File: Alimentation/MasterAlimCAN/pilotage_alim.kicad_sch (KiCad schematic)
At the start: 4 parts, among them U4 74LVC1G02

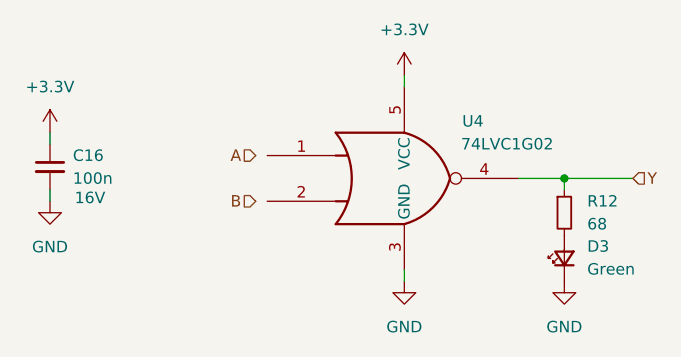
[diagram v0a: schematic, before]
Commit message: Restructure schematics of AlimCAN
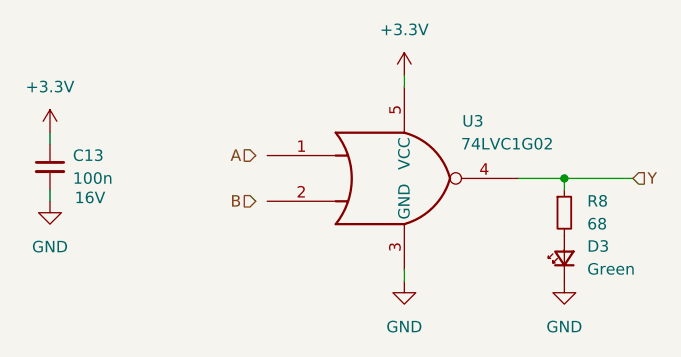
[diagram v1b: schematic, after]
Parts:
- renumbered C16 to C13, R12 to R8, U4 to U3
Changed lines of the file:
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@@
   (symbol (lib_id "power:GND") (at 246.38 123.19 0) (unit 1)
     (in_bom yes) (on_board yes) (dnp no) (fields_autoplaced)
-    (property "Reference" "#PWR053" (at 246.38 129.54 0)
+    (property "Reference" "#PWR035" (at 246.38 129.54 0)
       (effects (font (size 1.27 1.27)) hide)
     )
@@
     (instances
       (project "MasterAlimCAN"
-        (path "/c83bc042-587c-48f9-abdb-41233c8ec938/a6f4e771-72c9-4983-80a1-8951328e7346"
-          (reference "#PWR053") (unit 1)
-        )
-        (path "/c83bc042-587c-48f9-abdb-41233c8ec938/e65f16f5-16c4-48e9-9c3f-07516aed1840"
-          (reference "#PWR053") (unit 1)
-        )
-        (path "/c83bc042-587c-48f9-abdb-41233c8ec938/437897c5-9bcb-4226-b09d-80613b2e8e00"
-          (reference "#PWR053") (unit 1)
+        (path "/c83bc042-587c-48f9-abdb-41233c8ec938/2257b505-9461-4792-8707-8d13b64ba796/ef164321-3fd7-4989-9796-e8f2716b1c85"
+          (reference "#PWR035") (unit 1)
+        )
+        (path "/c83bc042-587c-48f9-abdb-41233c8ec938/2257b505-9461-4792-8707-8d13b64ba796/b62c8685-6929-45de-9238-6177db5cd56b"
+          (reference "#PWR040") (unit 1)
         )
       )
@@
   (symbol (lib_id "power:+3.3V") (at 189.23 106.68 0) (unit 1)
     (in_bom yes) (on_board yes) (dnp no) (fields_autoplaced)
-    (property "Reference" "#PWR049" (at 189.23 110.49 0)
+    (property "Reference" "#PWR031" (at 189.23 110.49 0)
       (effects (font (size 1.27 1.27)) hide)
     )
@@
     (instances
       (project "MasterAlimCAN"
-        (path "/c83bc042-587c-48f9-abdb-41233c8ec938/a6f4e771-72c9-4983-80a1-8951328e7346"
-          (reference "#PWR049") (unit 1)
-        )
-        (path "/c83bc042-587c-48f9-abdb-41233c8ec938/e65f16f5-16c4-48e9-9c3f-07516aed1840"
-          (reference "#PWR049") (unit 1)
-        )
-        (path "/c83bc042-587c-48f9-abdb-41233c8ec938/437897c5-9bcb-4226-b09d-80613b2e8e00"
-          (reference "#PWR049") (unit 1)
+        (path "/c83bc042-587c-48f9-abdb-41233c8ec938/2257b505-9461-4792-8707-8d13b64ba796/ef164321-3fd7-4989-9796-e8f2716b1c85"
+          (reference "#PWR031") (unit 1)
+        )
+        (path "/c83bc042-587c-48f9-abdb-41233c8ec938/2257b505-9461-4792-8707-8d13b64ba796/b62c8685-6929-45de-9238-6177db5cd56b"
+          (reference "#PWR036") (unit 1)
         )
       )
@@
   (symbol (lib_id "Device:R_Small") (at 246.38 115.57 0) (unit 1)
     (in_bom yes) (on_board yes) (dnp no) (fields_autoplaced)
-    (property "Reference" "R12" (at 248.92 114.3 0)
+    (property "Reference" "R8" (at 248.92 114.3 0)
       (effects (font (size 1.27 1.27)) (justify left))
     )
@@
     (instances
       (project "MasterAlimCAN"
-        (path "/c83bc042-587c-48f9-abdb-41233c8ec938/a6f4e771-72c9-4983-80a1-8951328e7346"
-          (reference "R12") (unit 1)
-        )
-        (path "/c83bc042-587c-48f9-abdb-41233c8ec938/437897c5-9bcb-4226-b09d-80613b2e8e00"
-          (reference "R12") (unit 1)
-        )
-        (path "/c83bc042-587c-48f9-abdb-41233c8ec938/e65f16f5-16c4-48e9-9c3f-07516aed1840"
-          (reference "R12") (unit 1)
+        (path "/c83bc042-587c-48f9-abdb-41233c8ec938/2257b505-9461-4792-8707-8d13b64ba796/ef164321-3fd7-4989-9796-e8f2716b1c85"
+          (reference "R8") (unit 1)
+        )
+        (path "/c83bc042-587c-48f9-abdb-41233c8ec938/2257b505-9461-4792-8707-8d13b64ba796/b62c8685-6929-45de-9238-6177db5cd56b"
+          (reference "R9") (unit 1)
         )
       )
@@
   (symbol (lib_id "power:GND") (at 228.6 123.19 0) (unit 1)
     (in_bom yes) (on_board yes) (dnp no) (fields_autoplaced)
-    (property "Reference" "#PWR052" (at 228.6 129.54 0)
+    (property "Reference" "#PWR034" (at 228.6 129.54 0)
       (effects (font (size 1.27 1.27)) hide)
     )
@@
     (instances
       (project "MasterAlimCAN"
-        (path "/c83bc042-587c-48f9-abdb-41233c8ec938/a6f4e771-72c9-4983-80a1-8951328e7346"
-          (reference "#PWR052") (unit 1)
-        )
-        (path "/c83bc042-587c-48f9-abdb-41233c8ec938/e65f16f5-16c4-48e9-9c3f-07516aed1840"
-          (reference "#PWR052") (unit 1)
-        )
-        (path "/c83bc042-587c-48f9-abdb-41233c8ec938/437897c5-9bcb-4226-b09d-80613b2e8e00"
-          (reference "#PWR052") (unit 1)
+        (path "/c83bc042-587c-48f9-abdb-41233c8ec938/2257b505-9461-4792-8707-8d13b64ba796/ef164321-3fd7-4989-9796-e8f2716b1c85"
+          (reference "#PWR034") (unit 1)
+        )
+        (path "/c83bc042-587c-48f9-abdb-41233c8ec938/2257b505-9461-4792-8707-8d13b64ba796/b62c8685-6929-45de-9238-6177db5cd56b"
+          (reference "#PWR039") (unit 1)
         )
       )
@@
   (symbol (lib_id "74xGxx:74LVC1G02") (at 228.6 111.76 0) (unit 1)
     (in_bom yes) (on_board yes) (dnp no)
-    (property "Reference" "U4" (at 236.22 105.41 0)
+    (property "Reference" "U3" (at 236.22 105.41 0)
       (effects (font (size 1.27 1.27)))
     )
@@
     (instances
       (project "MasterAlimCAN"
-        (path "/c83bc042-587c-48f9-abdb-41233c8ec938/a6f4e771-72c9-4983-80a1-8951328e7346"
-          (reference "U4") (unit 1)
-        )
-        (path "/c83bc042-587c-48f9-abdb-41233c8ec938/e65f16f5-16c4-48e9-9c3f-07516aed1840"
-          (reference "U4") (unit 1)
-        )
-        (path "/c83bc042-587c-48f9-abdb-41233c8ec938/437897c5-9bcb-4226-b09d-80613b2e8e00"
+        (path "/c83bc042-587c-48f9-abdb-41233c8ec938/2257b505-9461-4792-8707-8d13b64ba796/ef164321-3fd7-4989-9796-e8f2716b1c85"
+          (reference "U3") (unit 1)
+        )
+        (path "/c83bc042-587c-48f9-abdb-41233c8ec938/2257b505-9461-4792-8707-8d13b64ba796/b62c8685-6929-45de-9238-6177db5cd56b"
           (reference "U4") (unit 1)
         )
@@
     (instances
       (project "MasterAlimCAN"
-        (path "/c83bc042-587c-48f9-abdb-41233c8ec938/a6f4e771-72c9-4983-80a1-8951328e7346"
+        (path "/c83bc042-587c-48f9-abdb-41233c8ec938/2257b505-9461-4792-8707-8d13b64ba796/ef164321-3fd7-4989-9796-e8f2716b1c85"
           (reference "D3") (unit 1)
         )
-        (path "/c83bc042-587c-48f9-abdb-41233c8ec938/437897c5-9bcb-4226-b09d-80613b2e8e00"
-          (reference "D3") (unit 1)
-        )
-        (path "/c83bc042-587c-48f9-abdb-41233c8ec938/e65f16f5-16c4-48e9-9c3f-07516aed1840"
-          (reference "D3") (unit 1)
+        (path "/c83bc042-587c-48f9-abdb-41233c8ec938/2257b505-9461-4792-8707-8d13b64ba796/b62c8685-6929-45de-9238-6177db5cd56b"
+          (reference "D4") (unit 1)
         )
       )
@@
   (symbol (lib_id "power:+3.3V") (at 228.6 100.33 0) (unit 1)
     (in_bom yes) (on_board yes) (dnp no) (fields_autoplaced)
-    (property "Reference" "#PWR051" (at 228.6 104.14 0)
+    (property "Reference" "#PWR033" (at 228.6 104.14 0)
       (effects (font (size 1.27 1.27)) hide)
     )
@@
     (instances
       (project "MasterAlimCAN"
-        (path "/c83bc042-587c-48f9-abdb-41233c8ec938/a6f4e771-72c9-4983-80a1-8951328e7346"
-          (reference "#PWR051") (unit 1)
-        )
-        (path "/c83bc042-587c-48f9-abdb-41233c8ec938/e65f16f5-16c4-48e9-9c3f-07516aed1840"
-          (reference "#PWR051") (unit 1)
-        )
-        (path "/c83bc042-587c-48f9-abdb-41233c8ec938/437897c5-9bcb-4226-b09d-80613b2e8e00"
-          (reference "#PWR051") (unit 1)
+        (path "/c83bc042-587c-48f9-abdb-41233c8ec938/2257b505-9461-4792-8707-8d13b64ba796/ef164321-3fd7-4989-9796-e8f2716b1c85"
+          (reference "#PWR033") (unit 1)
+        )
+        (path "/c83bc042-587c-48f9-abdb-41233c8ec938/2257b505-9461-4792-8707-8d13b64ba796/b62c8685-6929-45de-9238-6177db5cd56b"
+          (reference "#PWR038") (unit 1)
         )
       )
@@
   (symbol (lib_id "Device:C_Small") (at 189.23 110.49 0) (unit 1)
     (in_bom yes) (on_board yes) (dnp no)
-    (property "Reference" "C16" (at 191.77 109.2263 0)
+    (property "Reference" "C13" (at 191.77 109.2263 0)
       (effects (font (size 1.27 1.27)) (justify left))
     )
@@
     (instances
       (project "MasterAlimCAN"
-        (path "/c83bc042-587c-48f9-abdb-41233c8ec938/a6f4e771-72c9-4983-80a1-8951328e7346"
-          (reference "C16") (unit 1)
-        )
-        (path "/c83bc042-587c-48f9-abdb-41233c8ec938/437897c5-9bcb-4226-b09d-80613b2e8e00"
-          (reference "C16") (unit 1)
-        )
-        (path "/c83bc042-587c-48f9-abdb-41233c8ec938/e65f16f5-16c4-48e9-9c3f-07516aed1840"
-          (reference "C16") (unit 1)
+        (path "/c83bc042-587c-48f9-abdb-41233c8ec938/2257b505-9461-4792-8707-8d13b64ba796/ef164321-3fd7-4989-9796-e8f2716b1c85"
+          (reference "C13") (unit 1)
+        )
+        (path "/c83bc042-587c-48f9-abdb-41233c8ec938/2257b505-9461-4792-8707-8d13b64ba796/b62c8685-6929-45de-9238-6177db5cd56b"
+          (reference "C14") (unit 1)
         )
       )
@@
   (symbol (lib_id "power:GND") (at 189.23 114.3 0) (unit 1)
     (in_bom yes) (on_board yes) (dnp no) (fields_autoplaced)
-    (property "Reference" "#PWR050" (at 189.23 120.65 0)
+    (property "Reference" "#PWR032" (at 189.23 120.65 0)
       (effects (font (size 1.27 1.27)) hide)
     )
@@
     (instances
       (project "MasterAlimCAN"
-        (path "/c83bc042-587c-48f9-abdb-41233c8ec938/a6f4e771-72c9-4983-80a1-8951328e7346"
-          (reference "#PWR050") (unit 1)
-        )
-        (path "/c83bc042-587c-48f9-abdb-41233c8ec938/e65f16f5-16c4-48e9-9c3f-07516aed1840"
-          (reference "#PWR050") (unit 1)
-        )
-        (path "/c83bc042-587c-48f9-abdb-41233c8ec938/437897c5-9bcb-4226-b09d-80613b2e8e00"
-          (reference "#PWR050") (unit 1)
-        )
-      )
+        (path "/c83bc042-587c-48f9-abdb-41233c8ec938/2257b505-9461-4792-8707-8d13b64ba796/ef164321-3fd7-4989-9796-e8f2716b1c85"
+          (reference "#PWR032") (unit 1)
+        )
+        (path "/c83bc042-587c-48f9-abdb-41233c8ec938/2257b505-9461-4792-8707-8d13b64ba796/b62c8685-6929-45de-9238-6177db5cd56b"
+          (reference "#PWR037") (unit 1)
+        )
+      )

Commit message: Init placement for MasterAlimCAN
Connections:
- net A: now also U3.1
- net B: now also U3.2
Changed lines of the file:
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@@
+    (stroke (width 0) (type default))
+  )
+  (wire (pts (xy 212.09 114.3) (xy 213.36 114.3))
+    (stroke (width 0) (type default))
+  )
+  (wire (pts (xy 212.09 109.22) (xy 213.36 109.22))
     (stroke (width 0) (type default))
   )
@@
   (symbol (lib_id "power:GND") (at 246.38 123.19 0) (unit 1)
     (in_bom yes) (on_board yes) (dnp no) (fields_autoplaced)
-    (property "Reference" "#PWR035" (at 246.38 129.54 0)
+    (property "Reference" "#PWR037" (at 246.38 129.54 0)
       (effects (font (size 1.27 1.27)) hide)
     )
@@
       (project "MasterAlimCAN"
         (path "/c83bc042-587c-48f9-abdb-41233c8ec938/2257b505-9461-4792-8707-8d13b64ba796/ef164321-3fd7-4989-9796-e8f2716b1c85"
-          (reference "#PWR035") (unit 1)
-        )
-        (path "/c83bc042-587c-48f9-abdb-41233c8ec938/2257b505-9461-4792-8707-8d13b64ba796/b62c8685-6929-45de-9238-6177db5cd56b"
-          (reference "#PWR040") (unit 1)
+          (reference "#PWR037") (unit 1)
+        )
+        (path "/c83bc042-587c-48f9-abdb-41233c8ec938/2257b505-9461-4792-8707-8d13b64ba796/b62c8685-6929-45de-9238-6177db5cd56b"
+          (reference "#PWR042") (unit 1)
         )
       )
@@
   (symbol (lib_id "power:+3.3V") (at 189.23 106.68 0) (unit 1)
     (in_bom yes) (on_board yes) (dnp no) (fields_autoplaced)
-    (property "Reference" "#PWR031" (at 189.23 110.49 0)
+    (property "Reference" "#PWR033" (at 189.23 110.49 0)
       (effects (font (size 1.27 1.27)) hide)
     )
@@
       (project "MasterAlimCAN"
         (path "/c83bc042-587c-48f9-abdb-41233c8ec938/2257b505-9461-4792-8707-8d13b64ba796/ef164321-3fd7-4989-9796-e8f2716b1c85"
-          (reference "#PWR031") (unit 1)
-        )
-        (path "/c83bc042-587c-48f9-abdb-41233c8ec938/2257b505-9461-4792-8707-8d13b64ba796/b62c8685-6929-45de-9238-6177db5cd56b"
+          (reference "#PWR033") (unit 1)
+        )
+        (path "/c83bc042-587c-48f9-abdb-41233c8ec938/2257b505-9461-4792-8707-8d13b64ba796/b62c8685-6929-45de-9238-6177db5cd56b"
+          (reference "#PWR038") (unit 1)
+        )
+      )
+    )
+  )
+  (symbol (lib_id "Device:R_Small") (at 246.38 115.57 0) (unit 1)
+    (in_bom yes) (on_board yes) (dnp no) (fields_autoplaced)
+    (property "Reference" "R8" (at 248.92 114.3 0)
+      (effects (font (size 1.27 1.27)) (justify left))
+    )
+    (property "Value" "68" (at 248.92 116.84 0)
+      (effects (font (size 1.27 1.27)) (justify left))
+    )
+    (property "Footprint" "Resistor_SMD:R_0805_2012Metric_Pad1.20x1.40mm_HandSolder" (at 246.38 115.57 0)
+      (effects (font (size 1.27 1.27)) hide)
+    )
+    (property "Datasheet" "~" (at 246.38 115.57 0)
+      (effects (font (size 1.27 1.27)) hide)
+    )
+    (property "LCSC Part" "C17802" (at 246.38 115.57 0)
+      (effects (font (size 1.27 1.27)) hide)
+    )
+    (pin "2")
+    (pin "1")
+    (instances
+      (project "MasterAlimCAN"
+        (path "/c83bc042-587c-48f9-abdb-41233c8ec938/2257b505-9461-4792-8707-8d13b64ba796/ef164321-3fd7-4989-9796-e8f2716b1c85"
+          (reference "R8") (unit 1)
+        )
+        (path "/c83bc042-587c-48f9-abdb-41233c8ec938/2257b505-9461-4792-8707-8d13b64ba796/b62c8685-6929-45de-9238-6177db5cd56b"
+          (reference "R9") (unit 1)
+        )
+      )
+    )
+  )
+  (symbol (lib_id "power:GND") (at 228.6 123.19 0) (unit 1)
+    (in_bom yes) (on_board yes) (dnp no) (fields_autoplaced)
+    (property "Reference" "#PWR036" (at 228.6 129.54 0)
+      (effects (font (size 1.27 1.27)) hide)
+    )
+    (property "Value" "GND" (at 228.6 128.27 0)
+      (effects (font (size 1.27 1.27)))
+    )
+    (property "Footprint" "" (at 228.6 123.19 0)
+      (effects (font (size 1.27 1.27)) hide)
+    )
+    (property "Datasheet" "" (at 228.6 123.19 0)
+      (effects (font (size 1.27 1.27)) hide)
+    )
+    (pin "1")
+    (instances
+      (project "MasterAlimCAN"
+        (path "/c83bc042-587c-48f9-abdb-41233c8ec938/2257b505-9461-4792-8707-8d13b64ba796/ef164321-3fd7-4989-9796-e8f2716b1c85"
           (reference "#PWR036") (unit 1)
         )
-      )
-    )
-  )
-  (symbol (lib_id "Device:R_Small") (at 246.38 115.57 0) (unit 1)
-    (in_bom yes) (on_board yes) (dnp no) (fields_autoplaced)
-    (property "Reference" "R8" (at 248.92 114.3 0)
-      (effects (font (size 1.27 1.27)) (justify left))
-    )
-    (property "Value" "68" (at 248.92 116.84 0)
-      (effects (font (size 1.27 1.27)) (justify left))
-    )
-    (property "Footprint" "Resistor_SMD:R_0805_2012Metric_Pad1.20x1.40mm_HandSolder" (at 246.38 115.57 0)
-      (effects (font (size 1.27 1.27)) hide)
-    )
-    (property "Datasheet" "~" (at 246.38 115.57 0)
-      (effects (font (size 1.27 1.27)) hide)
-    )
-    (property "LCSC Part" "C17802" (at 246.38 115.57 0)
-      (effects (font (size 1.27 1.27)) hide)
-    )
-    (pin "2")
-    (pin "1")
-    (instances
-      (project "MasterAlimCAN"
-        (path "/c83bc042-587c-48f9-abdb-41233c8ec938/2257b505-9461-4792-8707-8d13b64ba796/ef164321-3fd7-4989-9796-e8f2716b1c85"
-          (reference "R8") (unit 1)
-        )
-        (path "/c83bc042-587c-48f9-abdb-41233c8ec938/2257b505-9461-4792-8707-8d13b64ba796/b62c8685-6929-45de-9238-6177db5cd56b"
-          (reference "R9") (unit 1)
-        )
-      )
-    )
-  )
-  (symbol (lib_id "power:GND") (at 228.6 123.19 0) (unit 1)
-    (in_bom yes) (on_board yes) (dnp no) (fields_autoplaced)
-    (property "Reference" "#PWR034" (at 228.6 129.54 0)
-      (effects (font (size 1.27 1.27)) hide)
-    )
-    (property "Value" "GND" (at 228.6 128.27 0)
-      (effects (font (size 1.27 1.27)))
-    )
-    (property "Footprint" "" (at 228.6 123.19 0)
-      (effects (font (size 1.27 1.27)) hide)
-    )
-    (property "Datasheet" "" (at 228.6 123.19 0)
-      (effects (font (size 1.27 1.27)) hide)
-    )
-    (pin "1")
-    (instances
-      (project "MasterAlimCAN"
-        (path "/c83bc042-587c-48f9-abdb-41233c8ec938/2257b505-9461-4792-8707-8d13b64ba796/ef164321-3fd7-4989-9796-e8f2716b1c85"
-          (reference "#PWR034") (unit 1)
-        )
-        (path "/c83bc042-587c-48f9-abdb-41233c8ec938/2257b505-9461-4792-8707-8d13b64ba796/b62c8685-6929-45de-9238-6177db5cd56b"
-          (reference "#PWR039") (unit 1)
+        (path "/c83bc042-587c-48f9-abdb-41233c8ec938/2257b505-9461-4792-8707-8d13b64ba796/b62c8685-6929-45de-9238-6177db5cd56b"
+          (reference "#PWR041") (unit 1)
         )
       )
@@
   (symbol (lib_id "power:+3.3V") (at 228.6 100.33 0) (unit 1)
     (in_bom yes) (on_board yes) (dnp no) (fields_autoplaced)
-    (property "Reference" "#PWR033" (at 228.6 104.14 0)
+    (property "Reference" "#PWR035" (at 228.6 104.14 0)
       (effects (font (size 1.27 1.27)) hide)
     )
@@
       (project "MasterAlimCAN"
         (path "/c83bc042-587c-48f9-abdb-41233c8ec938/2257b505-9461-4792-8707-8d13b64ba796/ef164321-3fd7-4989-9796-e8f2716b1c85"
-          (reference "#PWR033") (unit 1)
-        )
-        (path "/c83bc042-587c-48f9-abdb-41233c8ec938/2257b505-9461-4792-8707-8d13b64ba796/b62c8685-6929-45de-9238-6177db5cd56b"
-          (reference "#PWR038") (unit 1)
+          (reference "#PWR035") (unit 1)
+        )
+        (path "/c83bc042-587c-48f9-abdb-41233c8ec938/2257b505-9461-4792-8707-8d13b64ba796/b62c8685-6929-45de-9238-6177db5cd56b"
+          (reference "#PWR040") (unit 1)
         )
       )
@@
   (symbol (lib_id "power:GND") (at 189.23 114.3 0) (unit 1)
     (in_bom yes) (on_board yes) (dnp no) (fields_autoplaced)
-    (property "Reference" "#PWR032" (at 189.23 120.65 0)
+    (property "Reference" "#PWR034" (at 189.23 120.65 0)
       (effects (font (size 1.27 1.27)) hide)
     )
@@
       (project "MasterAlimCAN"
         (path "/c83bc042-587c-48f9-abdb-41233c8ec938/2257b505-9461-4792-8707-8d13b64ba796/ef164321-3fd7-4989-9796-e8f2716b1c85"
-          (reference "#PWR032") (unit 1)
-        )
-        (path "/c83bc042-587c-48f9-abdb-41233c8ec938/2257b505-9461-4792-8707-8d13b64ba796/b62c8685-6929-45de-9238-6177db5cd56b"
-          (reference "#PWR037") (unit 1)
-        )
-      )
+          (reference "#PWR034") (unit 1)
+        )
+        (path "/c83bc042-587c-48f9-abdb-41233c8ec938/2257b505-9461-4792-8707-8d13b64ba796/b62c8685-6929-45de-9238-6177db5cd56b"
+          (reference "#PWR039") (unit 1)
+        )
+      )
